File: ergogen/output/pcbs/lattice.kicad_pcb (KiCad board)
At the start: 2 copper layers, 114.3 x 85.7 mm, 64 parts

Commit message: trying ch552t version
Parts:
- removed C3: , 100nF
- removed R3: , 1k
- removed SW1, SW2: , SW_Push
- removed U4: , XC6206PxxxMR
- turned MX1 to 180 degrees
- turned MX10 to 180 degrees
- turned MX11 to 180 degrees
- turned MX12 to 180 degrees
- turned MX13 to 180 degrees
- turned MX14 to 180 degrees
- turned MX15 to 180 degrees
- turned MX16 to 180 degrees
- turned MX17 to 180 degrees
- turned MX18 to 180 degrees
- turned MX19 to 180 degrees
- turned MX2 to 180 degrees
- turned MX20 to 180 degrees
- turned MX21 to 180 degrees
- turned MX22 to 180 degrees
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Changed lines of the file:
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@@
   (page A4)
   (title_block
-    (title lattice_left)
+    (title lattice)
     (rev 2024.03)
     (company sboysel)
@@
   )
         (module MX_SW_HS (layer B.Cu)
-            (at 95.25 114.3 0)
+            (at 95.25 114.3 180)
             (fp_text reference "MX1" (at 0 0 0) (layer "B.Fab")
               (effects (font (size 1 1) (thickness 0.15)))
@@
         )
         (module MX_SW_HS (layer B.Cu)
-            (at 95.25 95.25 0)
+            (at 95.25 95.25 180)
             (fp_text reference "MX2" (at 0 0 0) (layer "B.Fab")
               (effects (font (size 1 1) (thickness 0.15)))
@@
         )
         (module MX_SW_HS (layer B.Cu)
-            (at 95.25 76.2 0)
+            (at 95.25 76.2 180)
             (fp_text reference "MX3" (at 0 0 0) (layer "B.Fab")
               (effects (font (size 1 1) (thickness 0.15)))
@@
         )
         (module MX_SW_HS (layer B.Cu)
-            (at 95.25 57.150000000000006 0)
+            (at 95.25 57.150000000000006 180)
             (fp_text reference "MX4" (at 0 0 0) (layer "B.Fab")
               (effects (font (size 1 1) (thickness 0.15)))
@@
         )
         (module MX_SW_HS (layer B.Cu)
-            (at 114.3 114.3 0)
+            (at 114.3 114.3 180)
             (fp_text reference "MX5" (at 0 0 0) (layer "B.Fab")
               (effects (font (size 1 1) (thickness 0.15)))
@@
         )
         (module MX_SW_HS (layer B.Cu)
-            (at 114.3 95.25 0)
+            (at 114.3 95.25 180)
             (fp_text reference "MX6" (at 0 0 0) (layer "B.Fab")
               (effects (font (size 1 1) (thickness 0.15)))
@@
         )
         (module MX_SW_HS (layer B.Cu)
-            (at 114.3 76.2 0)
+            (at 114.3 76.2 180)
             (fp_text reference "MX7" (at 0 0 0) (layer "B.Fab")
               (effects (font (size 1 1) (thickness 0.15)))
@@
         )
         (module MX_SW_HS (layer B.Cu)
-            (at 114.3 57.150000000000006 0)
+            (at 114.3 57.150000000000006 180)
             (fp_text reference "MX8" (at 0 0 0) (layer "B.Fab")
               (effects (font (size 1 1) (thickness 0.15)))
@@
         )
         (module MX_SW_HS (layer B.Cu)
-            (at 133.35 114.3 0)
+            (at 133.35 114.3 180)
             (fp_text reference "MX9" (at 0 0 0) (layer "B.Fab")
               (effects (font (size 1 1) (thickness 0.15)))
@@
         )
         (module MX_SW_HS (layer B.Cu)
-            (at 133.35 95.25 0)
+            (at 133.35 95.25 180)
             (fp_text reference "MX10" (at 0 0 0) (layer "B.Fab")
               (effects (font (size 1 1) (thickness 0.15)))
@@
         )
         (module MX_SW_HS (layer B.Cu)
-            (at 133.35 76.2 0)
+            (at 133.35 76.2 180)
             (fp_text reference "MX11" (at 0 0 0) (layer "B.Fab")
               (effects (font (size 1 1) (thickness 0.15)))
@@
         )
         (module MX_SW_HS (layer B.Cu)
-            (at 133.35 57.150000000000006 0)
+            (at 133.35 57.150000000000006 180)
             (fp_text reference "MX12" (at 0 0 0) (layer "B.Fab")
               (effects (font (size 1 1) (thickness 0.15)))
@@
         )
         (module MX_SW_HS (layer B.Cu)
-            (at 152.4 114.3 0)
+            (at 152.4 114.3 180)
             (fp_text reference "MX13" (at 0 0 0) (layer "B.Fab")
               (effects (font (size 1 1) (thickness 0.15)))
@@
         )
         (module MX_SW_HS (layer B.Cu)
-            (at 152.4 95.25 0)
+            (at 152.4 95.25 180)
             (fp_text reference "MX14" (at 0 0 0) (layer "B.Fab")
               (effects (font (size 1 1) (thickness 0.15)))
@@
         )
         (module MX_SW_HS (layer B.Cu)
-            (at 152.4 76.2 0)
+            (at 152.4 76.2 180)
             (fp_text reference "MX15" (at 0 0 0) (layer "B.Fab")
               (effects (font (size 1 1) (thickness 0.15)))
@@
         )
         (module MX_SW_HS (layer B.Cu)
-            (at 152.4 57.150000000000006 0)
+            (at 152.4 57.150000000000006 180)
             (fp_text reference "MX16" (at 0 0 0) (layer "B.Fab")
               (effects (font (size 1 1) (thickness 0.15)))
@@
         )
         (module MX_SW_HS (layer B.Cu)
-            (at 171.45 114.3 0)
+            (at 171.45 114.3 180)
             (fp_text reference "MX17" (at 0 0 0) (layer "B.Fab")
               (effects (font (size 1 1) (thickness 0.15)))
@@
         )
         (module MX_SW_HS (layer B.Cu)
-            (at 171.45 95.25 0)
+            (at 171.45 95.25 180)
             (fp_text reference "MX18" (at 0 0 0) (layer "B.Fab")
               (effects (font (size 1 1) (thickness 0.15)))
@@
         )
         (module MX_SW_HS (layer B.Cu)
-            (at 171.45 76.2 0)
+            (at 171.45 76.2 180)
             (fp_text reference "MX19" (at 0 0 0) (layer "B.Fab")
               (effects (font (size 1 1) (thickness 0.15)))
@@
         )
         (module MX_SW_HS (layer B.Cu)
-            (at 171.45 57.150000000000006 0)
+            (at 171.45 57.150000000000006 180)
             (fp_text reference "MX20" (at 0 0 0) (layer "B.Fab")
               (effects (font (size 1 1) (thickness 0.15)))
@@
         )
         (module MX_SW_HS (layer B.Cu)
-            (at 190.5 114.3 0)
+            (at 190.5 114.3 180)
             (fp_text reference "MX21" (at 0 0 0) (layer "B.Fab")
               (effects (font (size 1 1) (thickness 0.15)))
@@
         )
         (module MX_SW_HS (layer B.Cu)
-            (at 190.5 95.25 0)
+            (at 190.5 95.25 180)
             (fp_text reference "MX22" (at 0 0 0) (layer "B.Fab")
               (effects (font (size 1 1) (thickness 0.15)))
@@
         )
         (module MX_SW_HS (layer B.Cu)
-            (at 190.5 76.2 0)
+            (at 190.5 76.2 180)
             (fp_text reference "MX23" (at 0 0 0) (layer "B.Fab")
               (effects (font (size 1 1) (thickness 0.15)))
@@
         )
         (module MX_SW_HS (layer B.Cu)
-            (at 190.5 57.150000000000006 0)
+            (at 190.5 57.150000000000006 180)
             (fp_text reference "MX24" (at 0 0 0) (layer "B.Fab")
               (effects (font (size 1 1) (thickness 0.15)))
@@
               (effects (font (size 1 1) (thickness 0.15)))
             )
-        )
-        (module XC6206PxxxMR (layer B.Cu)
-            (at 152.4 43.862500000000004 270)
-            (fp_text reference "U4" (at 0 0 0) (layer "B.Fab")
-              (effects (font (size 1 1) (thickness 0.15)))
-            )
-        )
-        (module 1k (layer B.Cu)
-            (at 147.4 47.62500000000001 90)
-            (fp_text reference "R3" (at 0 0 0) (layer "B.Fab")
-              (effects (font (size 1 1) (thickness 0.15)))
-            )
-        )
-        (module 100nF (layer B.Cu)
-            (at 148.4 47.62500000000001 90)
-            (fp_text reference "C3" (at 0 0 0) (layer "B.Fab")
-              (effects (font (size 1 1) (thickness 0.15)))
-            )
-        )
-        (module SW_Push (layer B.Cu)
-            (at 95.25 68.2 0)
-            (fp_text reference "SW1" (at 0 0 0) (layer "B.Fab")
-              (effects (font (size 1 1) (thickness 0.15)))
-            )
-        )
-        (module SW_Push (layer B.Cu)
-            (at 114.3 68.2 0)
-            (fp_text reference "SW2" (at 0 0 0) (layer "B.Fab")
-              (effects (font (size 1 1) (thickness 0.15)))
-            )

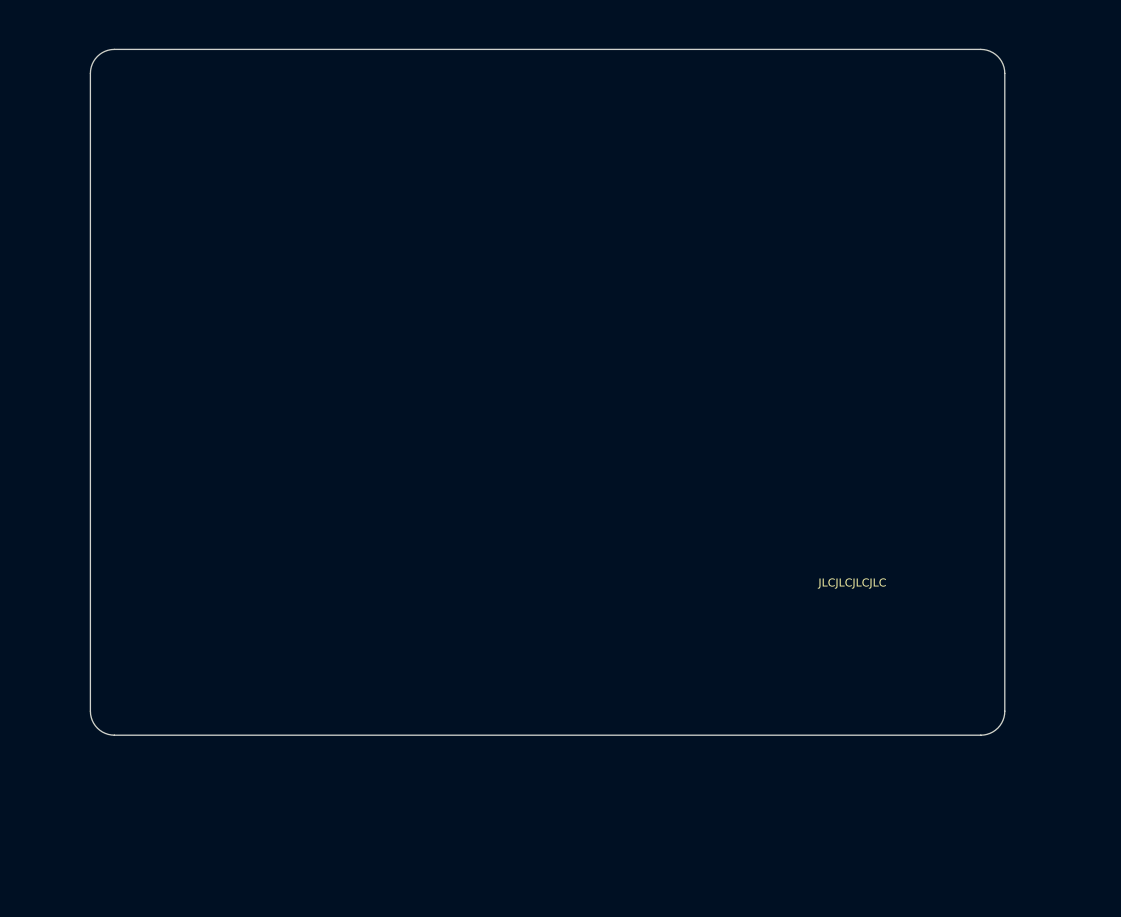
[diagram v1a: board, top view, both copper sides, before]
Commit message: more complete schematic
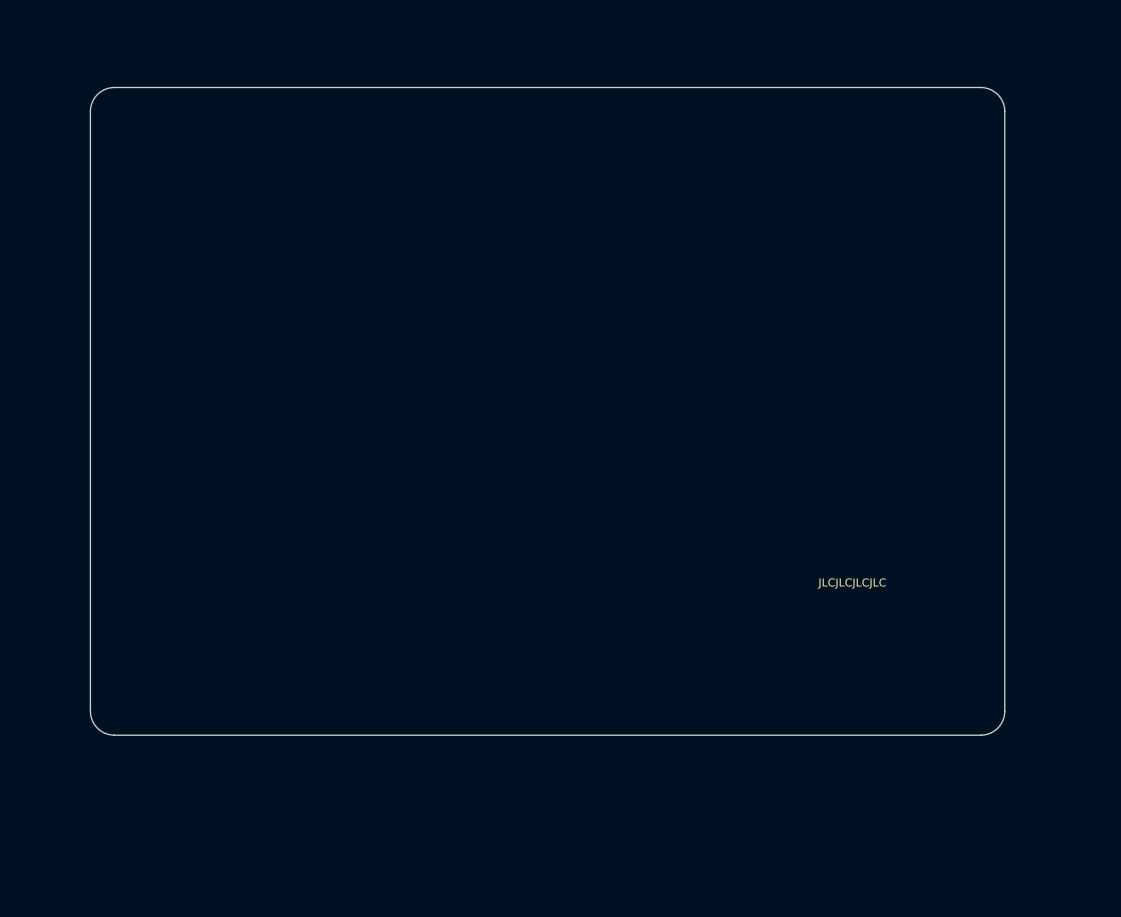
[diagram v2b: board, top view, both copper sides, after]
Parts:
- removed U3: , CH552T
- added F2: , 500mA, B.Cu at (181.0, 47.6)
- added R3: , 5k1, B.Cu at (181.0, 46.6)
- added R4: , 5k1, B.Cu at (181.0, 45.6)
- C1, C2: footprint 1uF -> 100n
- U1: footprint W25Q128JVS -> CH552T
- moved C1 34.7 mm to (139.3, 50.2), turned to 0 degrees
- moved C2 33.8 mm to (139.3, 51.2), turned to 0 degrees
- moved U2 33.7 mm to (142.9, 47.6)
- moved U1 29.0 mm to (133.3, 47.6), turned to 0 degrees
- moved D1 15.7 mm to (103.3, 114.3)
- moved D10 15.7 mm to (141.4, 95.2)
- moved D11 15.7 mm to (141.4, 76.2)
- moved D12 15.7 mm to (141.4, 57.2)
- moved D13 15.7 mm to (160.5, 114.3)
- moved D14 15.7 mm to (160.5, 95.2)
- moved D15 15.7 mm to (160.5, 76.2)
- moved D16 15.7 mm to (160.5, 57.2)
- moved D17 15.7 mm to (179.5, 114.3)
- moved D18 15.7 mm to (179.5, 95.2)
- moved D19 15.7 mm to (179.5, 76.2)
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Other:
- board size 114.3 x 85.7 mm -> 114.3 x 81 mm
- board text removed: "left"

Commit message: schematic work
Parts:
- added B1: , SW_SPST, B.Cu at (133.3, 69.2)
- added B2: , SW_SPST, B.Cu at (152.4, 69.2)
- added C3: , 100n, B.Cu at (134.3, 51.2)
- added R5: , 5k1, B.Cu at (181.0, 45.9)
- added R6: , 5k1, B.Cu at (181.0, 44.2)
- added SW1: , SW_Slide_DPDT, B.Cu at (114.3, 47.6)
- added SW2: , SW_Slide_DPDT, B.Cu at (142.9, 47.6)
- added SW3: , SW_Slide_DPDT, B.Cu at (171.4, 47.6)
- R3: footprint 5k1 -> 330R
- R4: footprint 5k1 -> 10k
- moved R3 58.5 mm to (126.3, 67.5), turned to 180 degrees
- moved R4 32.0 mm to (159.4, 69.2)
- moved C1 23.1 mm to (126.3, 69.2)
- moved D1 16.3 mm to (87.0, 114.3)
- moved D10 16.3 mm to (125.1, 95.2)
- moved D11 16.3 mm to (125.1, 76.2)
- moved D12 16.3 mm to (125.1, 57.2)
- moved D13 16.3 mm to (144.2, 114.3)
- moved D14 16.3 mm to (144.2, 95.2)
- moved D15 16.3 mm to (144.2, 76.2)
- moved D16 16.3 mm to (144.2, 57.2)
- moved D17 16.3 mm to (163.2, 114.3)
- moved D18 16.3 mm to (163.2, 95.2)
- moved D19 16.3 mm to (163.2, 76.2)
- moved D2 16.3 mm to (87.0, 95.2)
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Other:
- board text added: "lattice v2024.03"
- board text removed: "lattice v2024.02"

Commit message: schematic pretty solid
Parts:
- moved C2 1.22 mm to (135.3, 50.2)
- moved C3 1.12 mm to (135.3, 51.7)
- moved R2 0.40 mm to (104.8, 44.6)
- moved R6 0.40 mm to (181.0, 44.6)
- moved R1 0.20 mm to (104.8, 46.1)
- moved R3 0.20 mm to (126.3, 67.7)
- moved R5 0.20 mm to (181.0, 46.1)
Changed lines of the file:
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@@
         )
         (module 5k1 (layer B.Cu)
-            (at 104.775 45.925000000000004 0)
+            (at 104.775 46.12500000000001 0)
             (fp_text reference "R1" (at 0 0 0) (layer "B.Fab")
               (effects (font (size 1 1) (thickness 0.15)))
@@
         )
         (module 5k1 (layer B.Cu)
-            (at 104.775 44.22500000000001 0)
+            (at 104.775 44.62500000000001 0)
             (fp_text reference "R2" (at 0 0 0) (layer "B.Fab")
               (effects (font (size 1 1) (thickness 0.15)))
@@
         )
         (module 330R (layer B.Cu)
-            (at 126.35 67.5 180)
+            (at 126.35 67.7 180)
             (fp_text reference "R3" (at 0 0 0) (layer "B.Fab")
               (effects (font (size 1 1) (thickness 0.15)))
@@
         )
         (module 100n (layer B.Cu)
-            (at 134.35 49.45 0)
+            (at 135.35 50.150000000000006 0)
             (fp_text reference "C2" (at 0 0 0) (layer "B.Fab")
               (effects (font (size 1 1) (thickness 0.15)))
@@
         )
         (module 100n (layer B.Cu)
-            (at 134.35 51.150000000000006 0)
+            (at 135.35 51.650000000000006 0)
             (fp_text reference "C3" (at 0 0 0) (layer "B.Fab")
               (effects (font (size 1 1) (thickness 0.15)))
@@
         )
         (module 5k1 (layer B.Cu)
-            (at 180.975 45.925000000000004 0)
+            (at 180.975 46.12500000000001 0)
             (fp_text reference "R5" (at 0 0 0) (layer "B.Fab")
               (effects (font (size 1 1) (thickness 0.15)))
@@
         )
         (module 5k1 (layer B.Cu)
-            (at 180.975 44.22500000000001 0)
+            (at 180.975 44.62500000000001 0)
             (fp_text reference "R6" (at 0 0 0) (layer "B.Fab")
               (effects (font (size 1 1) (thickness 0.15)))
